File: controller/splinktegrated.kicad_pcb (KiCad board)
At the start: 2 copper layers, 26 x 41.6 mm, 45 parts, among them J1 USB_C_Receptacle_USB2.0, J11 Conn_01x07_Socket, J2 Conn_01x04_Socket, J5 Conn_01x02, J7 Cirque, U1 RP2040, U3 XC6210B332MR-G, U4 USBLC6-2P6, U5 W25Q128JVS, Y1 Crystal_GND24

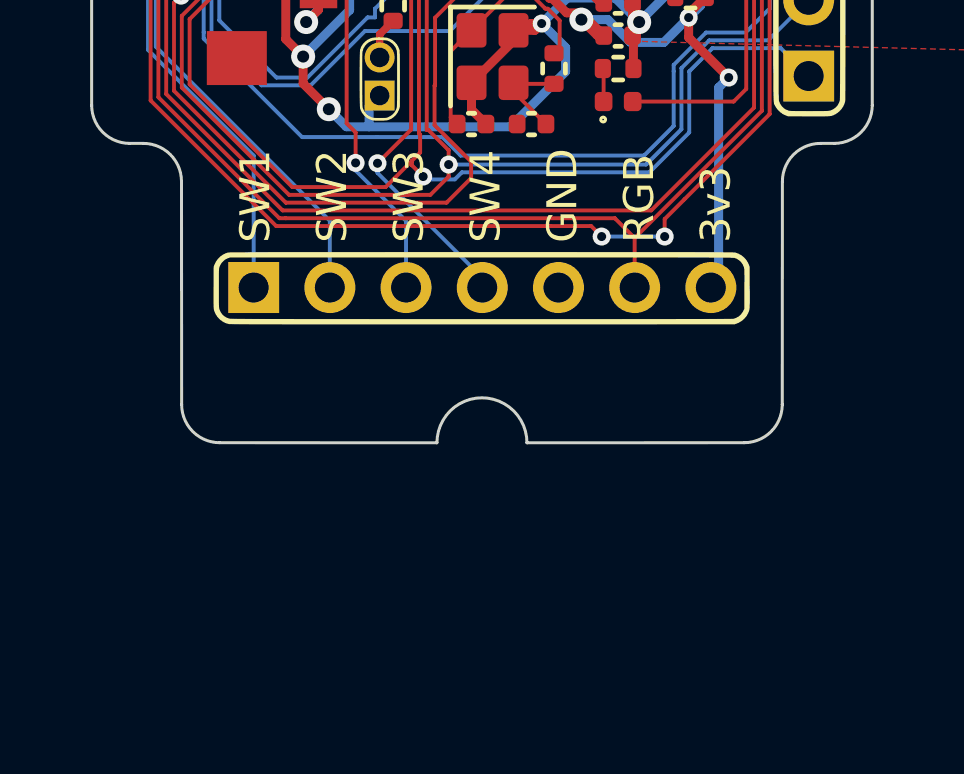
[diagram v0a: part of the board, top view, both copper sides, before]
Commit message: 5mm longer controller
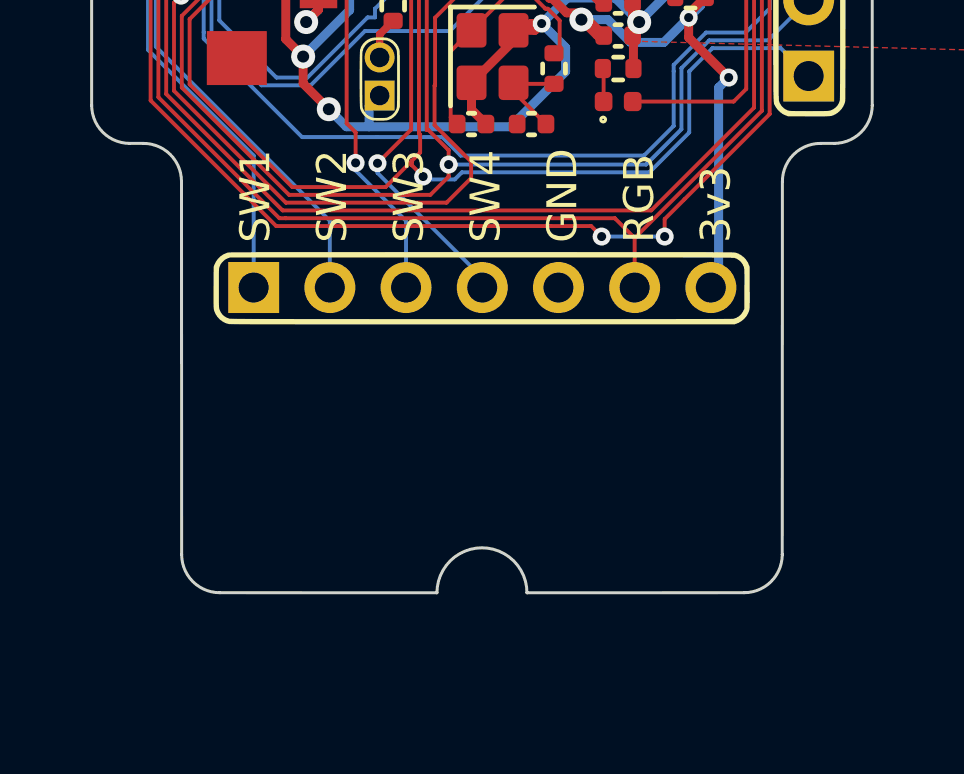
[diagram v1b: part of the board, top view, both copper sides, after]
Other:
- board size 26 x 41.6 mm -> 26 x 46.6 mm
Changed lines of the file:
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@@
 	)
 	(gr_line
-		(start 162.42 116.501945)
+		(start 162.42 121.501945)
 		(end 162.4251 109.065)
 		(stroke
@@
 	)
 	(gr_arc
-		(start 150.91 117.775)
-		(mid 152.41 116.275)
-		(end 153.91 117.775)
+		(start 150.91 122.775)
+		(mid 152.41 121.275)
+		(end 153.91 122.775)
 		(stroke
 			(width 0.1)
@@
 	(gr_line
 		(start 142.3949 109.065)
-		(end 142.4 116.501945)
+		(end 142.4 121.501945)
 		(stroke
 			(width 0.1)
@@
 	)
 	(gr_line
-		(start 143.67 117.771945)
-		(end 150.91 117.775)
+		(start 143.67 122.771945)
+		(end 150.91 122.775)
 		(stroke
 			(width 0.1)
@@
 	)
 	(gr_arc
-		(start 162.42 116.501945)
-		(mid 162.048042 117.399987)
-		(end 161.15 117.771945)
+		(start 162.42 121.501945)
+		(mid 162.048039 122.399971)
+		(end 161.15 122.771945)
 		(stroke
 			(width 0.1)
@@
 	)
 	(gr_line
-		(start 153.91 117.775)
-		(end 161.15 117.771945)
+		(start 153.91 122.775)
+		(end 161.15 122.771945)
 		(stroke
 			(width 0.1)
@@
 	)
 	(gr_arc
-		(start 143.67 117.771945)
-		(mid 142.771945 117.4)
-		(end 142.4 116.501945)
+		(start 143.67 122.771945)
+		(mid 142.771929 122.400003)
+		(end 142.4 121.501945)
 		(stroke
 			(width 0.1)
@@
 	)
 	(gr_circle
-		(center 152.41 117.775)
-		(end 155.4 117.2)
+		(center 152.41 122.775)
+		(end 155.4 122.2)
 		(stroke
 			(width 0.15)

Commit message: revert connector
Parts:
- moved J11 15.2 mm to (160.0, 112.6), turned to -90 degrees
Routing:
- net +3V3: track 119.8 -> 138.6 mm
- net RGB: track 48.1 -> 61.8 mm
- net sw1: track 30.9 -> 42.3 mm
- net sw2: track 31.5 -> 41.4 mm
- net sw3: track 15.8 -> 23.7 mm
- net sw4: track 15.4 -> 21.6 mm
- net /GP26: track 43.1 -> 40.6 mm

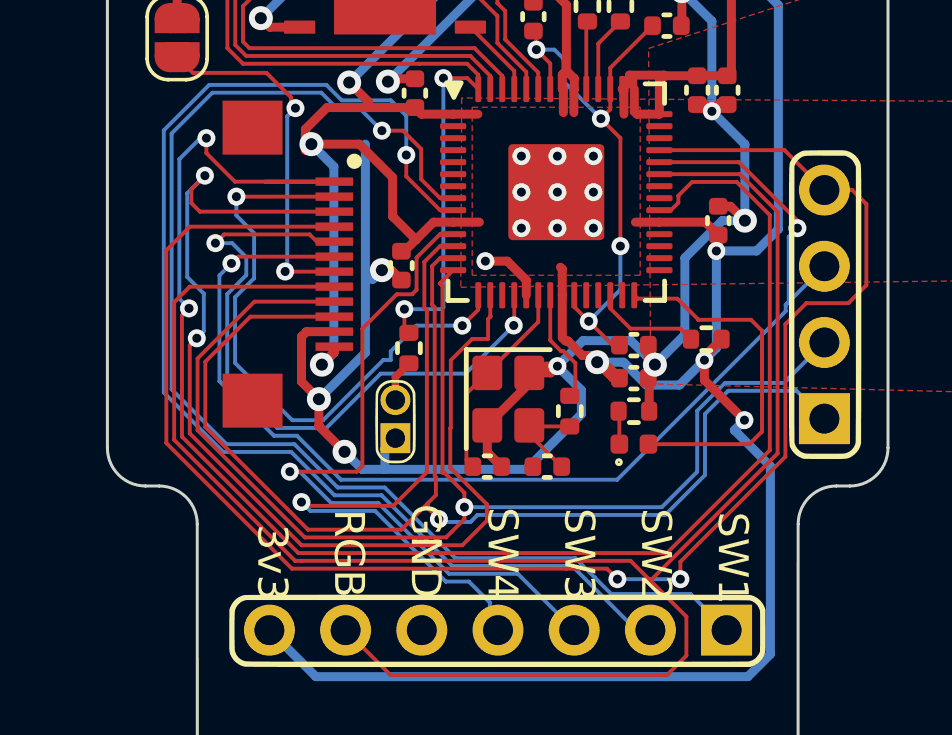
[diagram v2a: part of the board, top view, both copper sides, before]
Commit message: change SCK pin
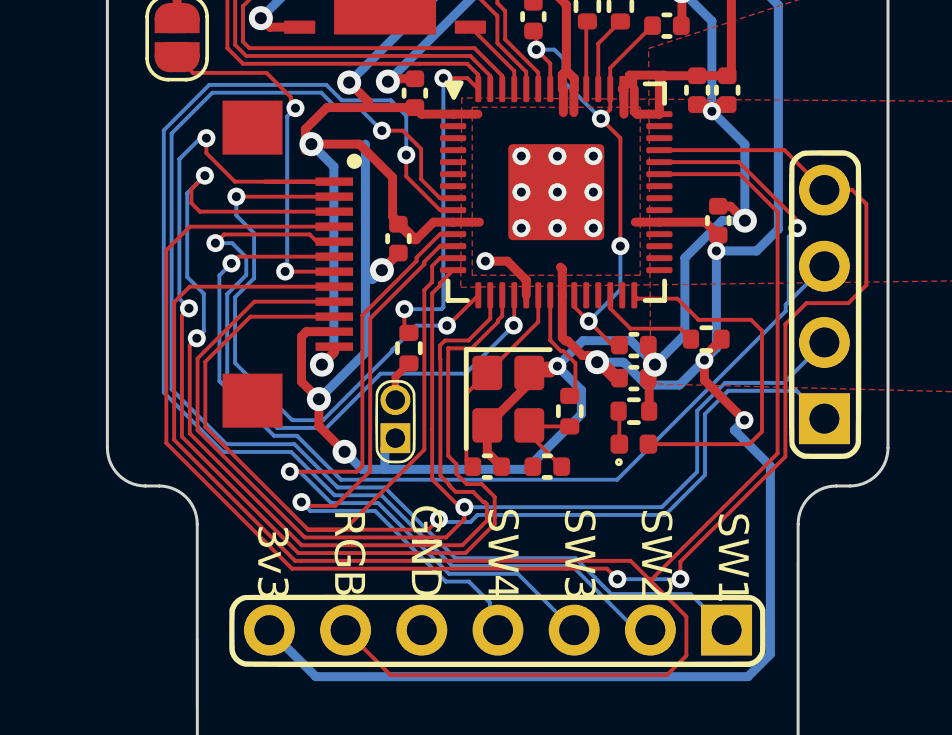
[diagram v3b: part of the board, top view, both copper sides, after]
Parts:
- moved C9 0.91 mm to (149.1, 99.5)
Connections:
- U1 pad 17: unconnected-(U1-GPIO14-Pad17) -> /SCLK
- U1 pad 34: /SCLK -> unconnected-(U1-GPIO22-Pad34)
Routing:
- net /SCLK: track 53.3 -> 40.3 mm
- net SDA: track 42.1 -> 44.7 mm
- net sw4: track 21.6 -> 20.4 mm
- net NCS: track 35.9 -> 36.7 mm

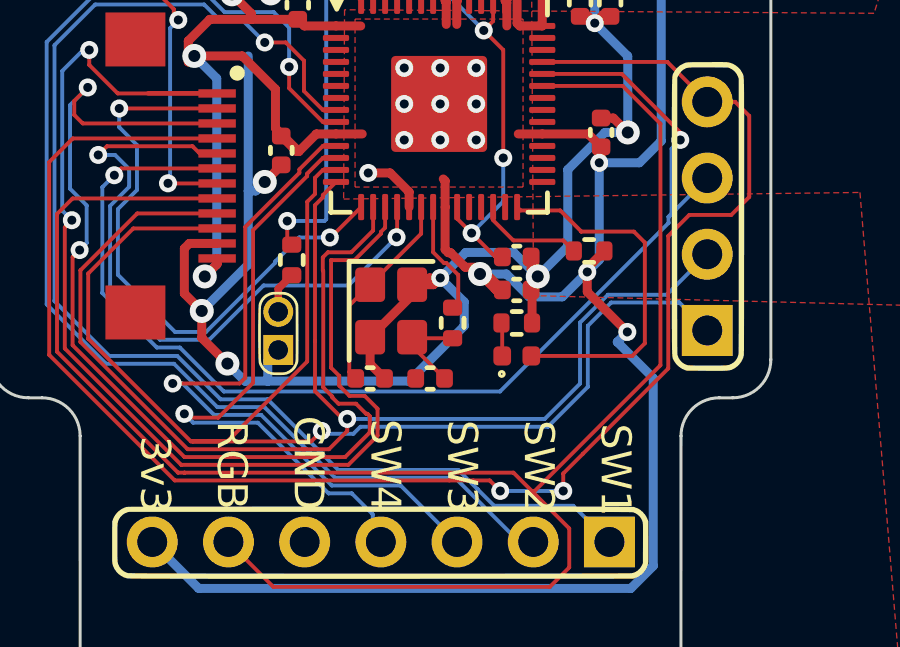
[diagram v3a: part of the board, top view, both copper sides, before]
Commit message: update USB BOM
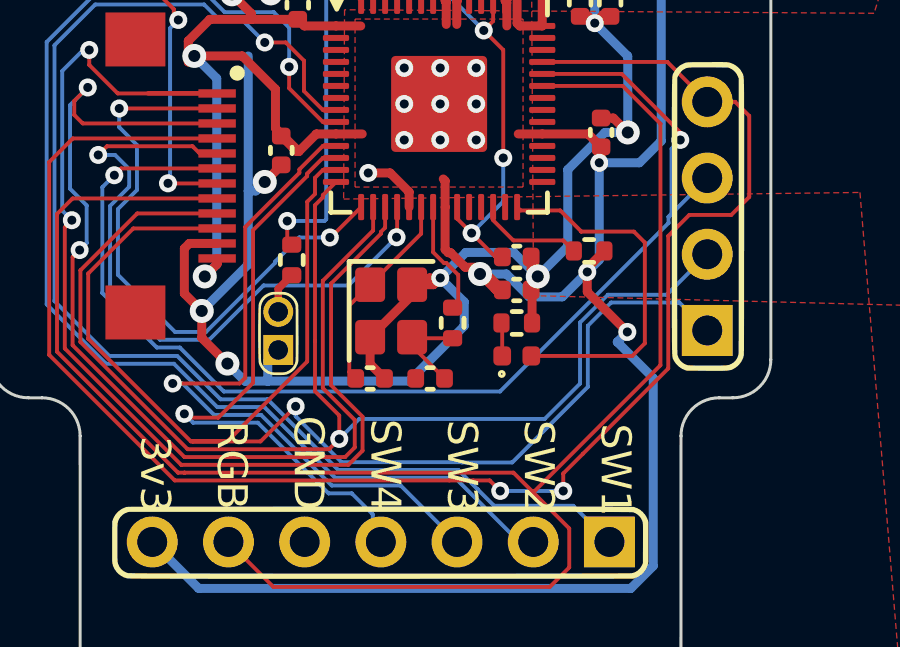
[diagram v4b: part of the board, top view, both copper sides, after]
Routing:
- net SDA: track 44.7 -> 46.4 mm
- net NCS: track 36.7 -> 35.5 mm
- net /SCLK: track 40.3 -> 39.2 mm

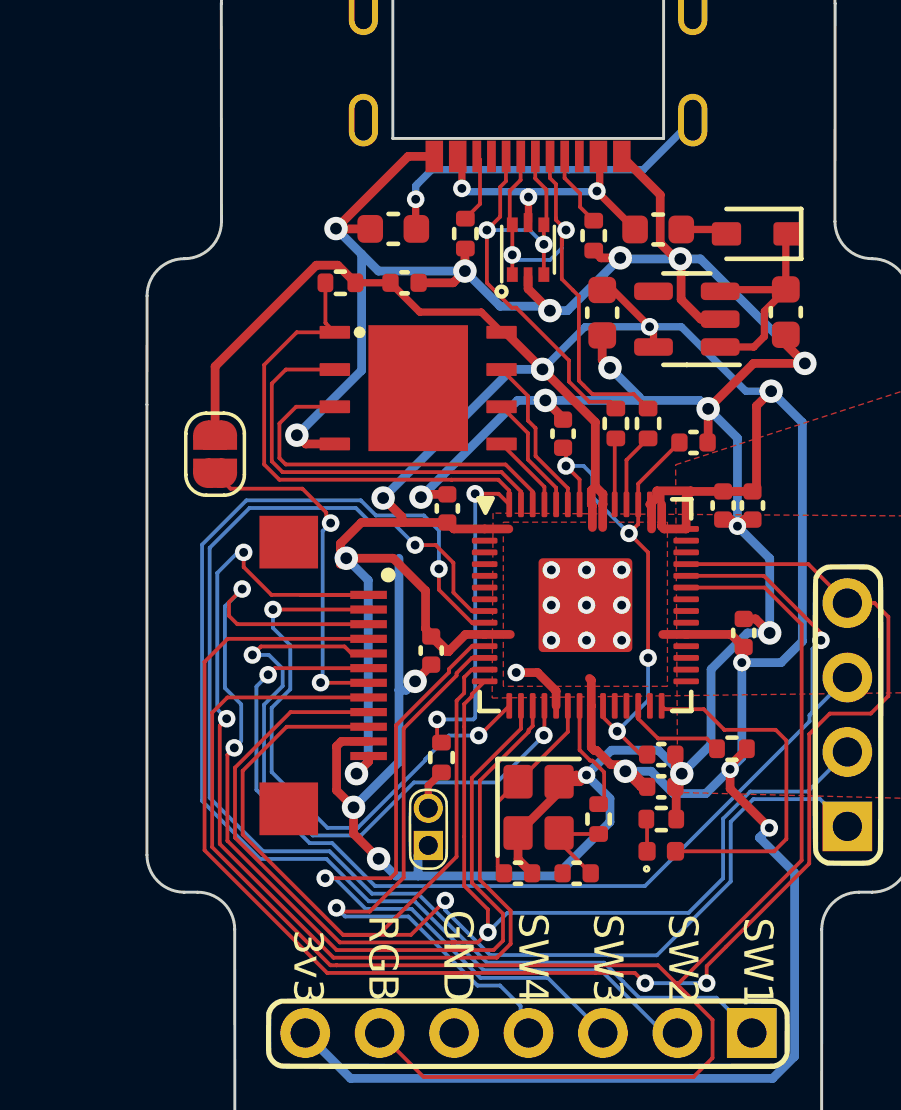
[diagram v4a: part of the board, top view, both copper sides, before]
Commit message: add trackpad breakouts
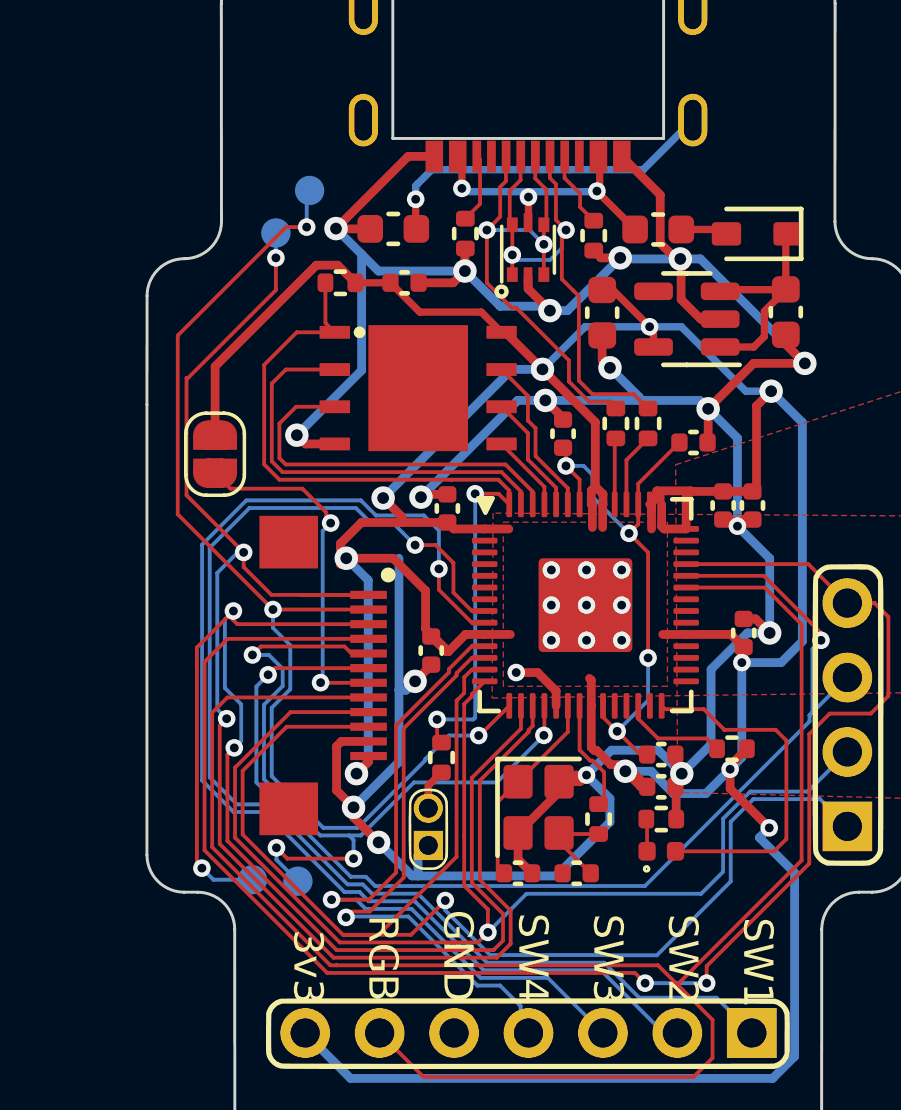
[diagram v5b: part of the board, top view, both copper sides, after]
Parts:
- added J3: Conn_01x01_Socket, drawings:PinHeader_1x01_P1.27mm_SMD, B.Cu at (144.6, 106.2)
- added J4: Conn_01x01_Socket, drawings:PinHeader_1x01_P1.27mm_SMD, B.Cu at (143.0, 106.1)
- added J6: Conn_01x01_Socket, drawings:PinHeader_1x01_P1.27mm_SMD, B.Cu at (144.9, 82.6)
- added J8: Conn_01x01_Socket, drawings:PinHeader_1x01_P1.27mm_SMD, B.Cu at (143.8, 84.0)
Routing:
- net /MISO: track 20.0 -> 38.0 mm, vias 2 -> 3
- net /SCLK: track 39.2 -> 52.2 mm, vias 2 -> 3
- net NCS: track 35.5 -> 45.0 mm, vias 2 -> 3
- net /MOSI: track 22.4 -> 27.3 mm, vias 2 -> 4
- net sw4: track 20.4 -> 19.7 mm
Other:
- board text added: "MISO"
- board text added: "MOSI"
- board text added: "NCS"
- board text added: "SCK"

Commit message: version number
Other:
- board text added: "ARGOS CONTROLLER REV 1.1"
- board text removed: "ARGOS CONTROLLER REV 1.0"
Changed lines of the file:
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@@
 		)
 	)
-	(gr_text "ARGOS CONTROLLER REV 1.0"
+	(gr_text "ARGOS CONTROLLER REV 1.1"
 		(at 142.05 87.5 90)
 		(layer "B.SilkS")
@@
 			(justify left bottom mirror)
 		)
-		(render_cache "ARGOS CONTROLLER REV 1.0" 90
+		(render_cache "ARGOS CONTROLLER REV 1.1" 90
 			(polygon
 				(pts
@@
 			(polygon
 				(pts
-					(xy 141.666648 104.606979) (xy 141.715741 104.617365) (xy 141.767648 104.637055) (xy 141.79052 104.649849)
-					(xy 141.829515 104.681042) (xy 141.859511 104.719705) (xy 141.880508 104.765838) (xy 141.892506 104.819442)
-					(xy 141.895631 104.869818) (xy 141.895131 104.890857) (xy 141.889507 104.941619) (xy 141.877633 104.989757)
-					(xy 141.859511 105.035271) (xy 141.835139 105.078161) (xy 141.804518 105.118428) (xy 141.767648 105.156071)
-					(xy 141.751195 105.170341) (xy 141.706347 105.20372) (xy 141.656193 105.23382) (xy 141.612248 105.255539)
-					(xy 141.564907 105.275158) (xy 141.51417 105.292679) (xy 141.460035 105.3081) (xy 141.402505 105.321423)
-					(xy 141.358833 105.329728) (xy 141.303649 105.337715) (xy 141.251946 105.342177) (xy 141.192212 105.342794)
-					(xy 141.137915 105.337902) (xy 141.089057 105.327501) (xy 141.037606 105.307745) (xy 141.022256 105.299421)
-					(xy 140.982148 105.269445) (xy 140.946619 105.224988) (xy 140.925823 105.178752) (xy 140.913939 105.125011)
-					(xy 140.910844 105.074494) (xy 140.910968 105.063952) (xy 140.91293 105.040788) (xy 141.073021 105.040788)
-					(xy 141.075883 105.067464) (xy 141.10233 105.108688) (xy 141.104204 105.110008) (xy 141.152203 105.125945)
-					(xy 141.203691 105.128227) (xy 141.243045 105.125815) (xy 141.295565 105.119379) (xy 141.349581 105.11035)
-					(xy 141.402505 105.099895) (xy 141.45544 105.088273) (xy 141.503117 105.076487) (xy 141.551164 105.062817)
-					(xy 141.601563 105.045429) (xy 141.618862 105.038376) (xy 141.662929 105.01612) (xy 141.703412 104.983879)
-					(xy 141.723948 104.951909) (xy 141.733454 104.903524) (xy 141.730448 104.877105) (xy 141.702679 104.836113)
-					(xy 141.698672 104.833576) (xy 141.651669 104.819177) (xy 141.600097 104.816817) (xy 141.56082 104.819306)
-					(xy 141.508568 104.825718) (xy 141.454953 104.834629) (xy 141.402505 104.844905) (xy 141.357342 104.854766)
-					(xy 141.303082 104.8681) (xy 141.25563 104.881648) (xy 141.205889 104.898883) (xy 141.188693 104.905993)
-					(xy 141.144706 104.928375) (xy 141.103796 104.960676) (xy 141.082758 104.99272) (xy 141.073021 105.040788)
-					(xy 140.91293 105.040788) (xy 140.9153 105.012801) (xy 140.925823 104.964251) (xy 140.946619 104.909422)
-					(xy 140.970759 104.866591) (xy 141.001088 104.82636) (xy 141.037606 104.788729) (xy 141.053886 104.774487)
-					(xy 141.098394 104.741152) (xy 141.14834 104.71106) (xy 141.192212 104.689323) (xy 141.239564 104.669661)
-					(xy 141.290397 104.652076) (xy 141.344711 104.636566) (xy 141.402505 104.623133) (xy 141.445971 104.614913)
-					(xy 141.500954 104.607019) (xy 141.552541 104.602629) (xy 141.612248 104.602067)
-				)
-			)
+					(xy 140.942107 105.068876) (xy 141.88 104.87397) (xy 141.88 104.661723) (xy 141.161681 104.810956)
+					(xy 141.284047 104.586985) (xy 141.139455 104.522505) (xy 140.942107 104.87568)
+				)
+			)
